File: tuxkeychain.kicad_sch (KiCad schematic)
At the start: 45 parts, among them J1 Amphenol_10104111, Q2 2N7002, SW1 B3U-1000P, U1 JW5211, U2 JW5211, U3 JW5211, U4 F1C100s, U6 W25Q128JVS, Y1 24MHz

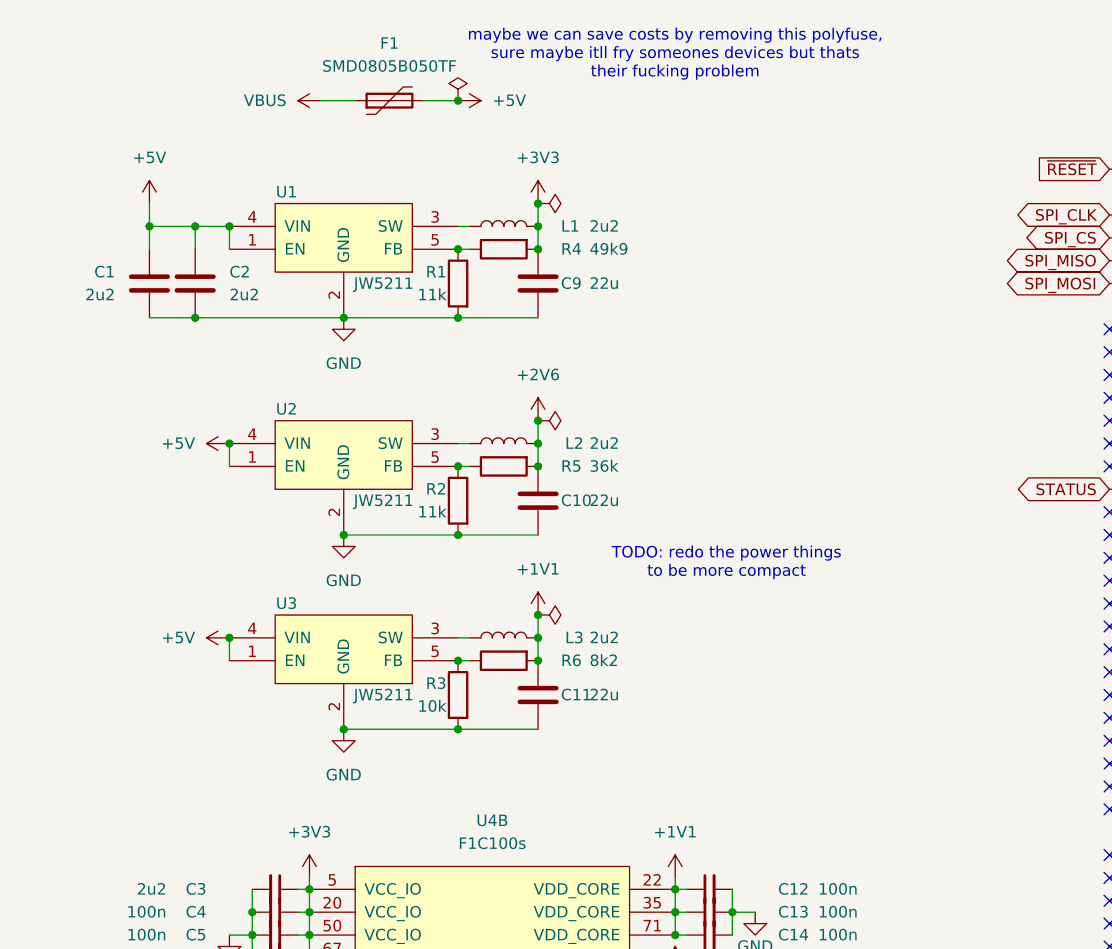
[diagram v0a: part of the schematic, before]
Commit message: Change regulators to the TLV76701DRVx due to supply chain issues
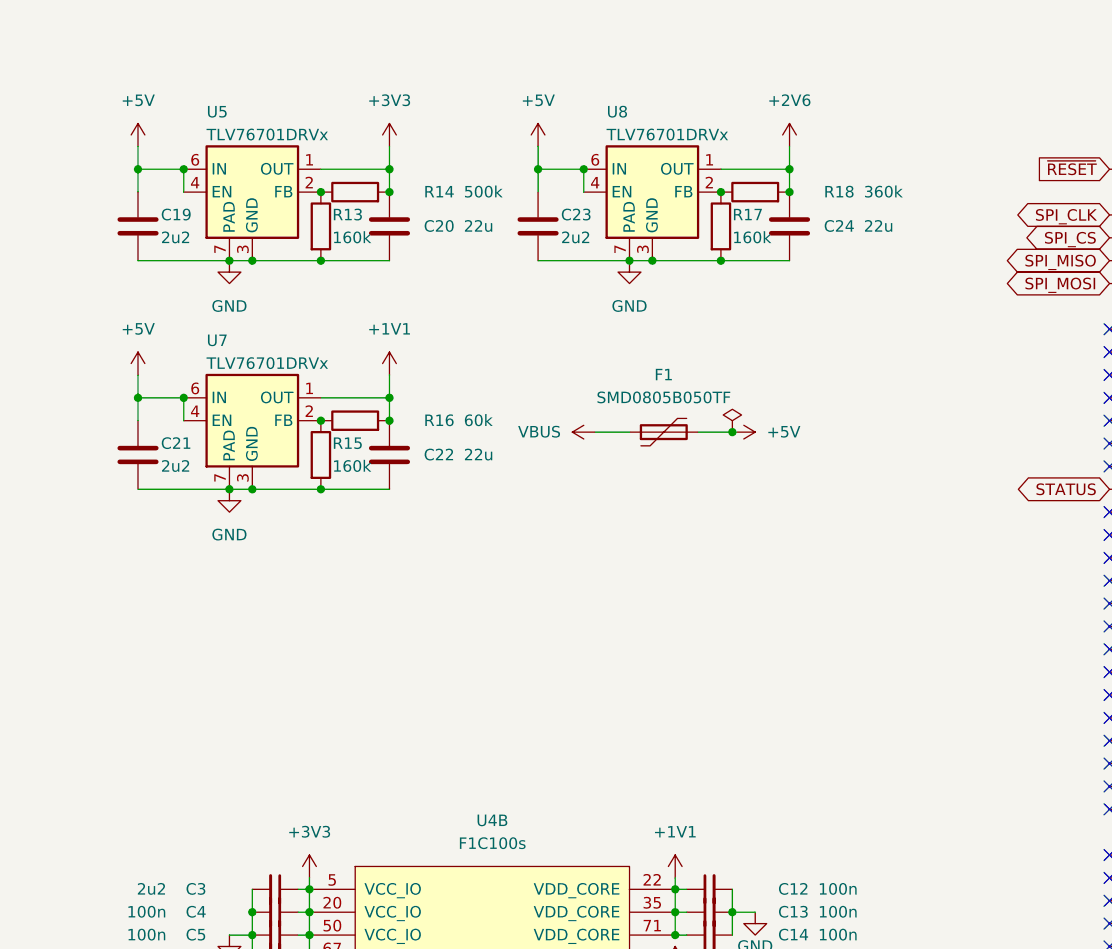
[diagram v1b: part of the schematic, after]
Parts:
- removed C1, C2: 2u2, Capacitor_SMD:C_0603_1608Metric, symbol Device:C
- removed C10, C11, C9: 22u, Capacitor_SMD:C_0603_1608Metric, symbol Device:C
- removed L1, L2, L3: 2u2, Inductor_SMD:L_0805_2012Metric, symbol Device:L
- removed R1, R2: 11k, Resistor_SMD:R_0603_1608Metric, symbol Device:R
- removed R3: 10k, Resistor_SMD:R_0603_1608Metric, symbol Device:R
- removed R4: 49k9, Resistor_SMD:R_0603_1608Metric, symbol Device:R
- removed R5: 36k, Resistor_SMD:R_0603_1608Metric, symbol Device:R
- removed R6: 8k2, Resistor_SMD:R_0603_1608Metric, symbol Device:R
- removed U1, U2, U3: JW5211, Package_TO_SOT_SMD:SOT-23-5, symbol tuxkeychain:JW5211
- added C19, C21, C23: 2u2, Capacitor_SMD:C_0603_1608Metric, symbol Device:C
- added C20, C22, C24: 22u, symbol Device:C
- added R13, R15, R17: 160k, symbol Device:R
- added R14: 500k, symbol Device:R
- added R16: 60k, symbol Device:R
- added R18: 360k, symbol Device:R
- added U5, U7, U8: TLV76701DRVx, Package_SON:WSON-6-1EP_2x2mm_P0.65mm_EP1x1.6mm, symbol Regulator_Linear:TLV76701DRVx
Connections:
- net +1V1: now also C22.1, R16.2, U7.1 (OUT)
- net +2V6: now also C24.1, R18.2, U8.1 (OUT)
- net +3V3: now also C20.1, R14.2, U5.1 (OUT)
- net +5V: now also C19.1, C21.1, C23.1, U5.4 (EN), U5.6 (IN), U7.4 (EN), U7.6 (IN), U8.4 (EN), U8.6 (IN)
- net GND: now also C19.2, C20.2, C21.2, C22.2, C23.2, C24.2, R13.2, R15.2, R17.2, U5.3 (GND), U5.5 (GND), U5.7 (PAD), U7.3 (GND), U7.5 (GND), U7.7 (PAD), U8.3 (GND), U8.5 (GND), U8.7 (PAD)
- new net: R13.1, R14.1, U5.2 (FB)
- new net: R17.1, R18.1, U8.2 (FB)
- new net: R15.1, R16.1, U7.2 (FB)
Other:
- note removed: "TODO: redo the power things to be more compact"
- note removed: "maybe we can save costs by removing this polyfuse, sure maybe itll fry someones devices but thats their fucking problem"
- moved on the sheet: F1

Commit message: bump rev
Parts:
- removed C19, C21, C23: 2u2, Capacitor_SMD:C_0603_1608Metric, symbol Device:C
- removed C20, C22, C24: 22u, symbol Device:C
- removed R13, R15, R17: 160k, symbol Device:R
- removed R14: 500k, symbol Device:R
- removed R16: 60k, symbol Device:R
- removed R18: 360k, symbol Device:R
- removed U5, U7, U8: TLV76701DRVx, Package_SON:WSON-6-1EP_2x2mm_P0.65mm_EP1x1.6mm, symbol Regulator_Linear:TLV76701DRVx
- added C1, C2: 2u2, Capacitor_SMD:C_0603_1608Metric, symbol Device:C
- added C10, C11, C9: 22u, Capacitor_SMD:C_0603_1608Metric, symbol Device:C
- added L1, L2, L3: 2u2, Inductor_SMD:L_0805_2012Metric, symbol Device:L
- added R1, R2: 11k, Resistor_SMD:R_0603_1608Metric, symbol Device:R
- added R3: 10k, Resistor_SMD:R_0603_1608Metric, symbol Device:R
- added R4: 49k9, Resistor_SMD:R_0603_1608Metric, symbol Device:R
- added R5: 36k, Resistor_SMD:R_0603_1608Metric, symbol Device:R
- added R6: 8k2, Resistor_SMD:R_0603_1608Metric, symbol Device:R
- added U1, U2, U3: JW5211, Package_TO_SOT_SMD:SOT-23-5, symbol tuxkeychain:JW5211
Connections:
- net +1V1: now also C11.1, L3.2, R6.2
- net +2V6: now also C10.1, L2.2, R5.2
- net +3V3: now also C9.1, L1.2, R4.2
- net +5V: now also C1.1, C2.1, U1.1 (EN), U1.4 (VIN), U2.1 (EN), U2.4 (VIN), U3.1 (EN), U3.4 (VIN)
- net GND: now also C1.2, C10.2, C11.2, C2.2, C9.2, R1.2, R2.2, R3.2, U1.2 (GND), U2.2 (GND), U3.2 (GND)
- new net: L2.1, U2.3 (SW)
- new net: R1.1, R4.1, U1.5 (FB)
- new net: R3.1, R6.1, U3.5 (FB)
- new net: L1.1, U1.3 (SW)
- new net: L3.1, U3.3 (SW)
- new net: R2.1, R5.1, U2.5 (FB)
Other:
- note added: "TODO: redo the power things to be more compact"
- note added: "maybe we can save costs by removing this polyfuse, sure maybe itll fry someones devices but thats their fucking problem"
- moved on the sheet: F1

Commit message: Revert "bump rev"
This reverts commit ef9e417096638242890c258b05ee16d024b64b77.
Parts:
- removed C1, C2: 2u2, Capacitor_SMD:C_0603_1608Metric, symbol Device:C
- removed C10, C11, C9: 22u, Capacitor_SMD:C_0603_1608Metric, symbol Device:C
- removed L1, L2, L3: 2u2, Inductor_SMD:L_0805_2012Metric, symbol Device:L
- removed R1, R2: 11k, Resistor_SMD:R_0603_1608Metric, symbol Device:R
- removed R3: 10k, Resistor_SMD:R_0603_1608Metric, symbol Device:R
- removed R4: 49k9, Resistor_SMD:R_0603_1608Metric, symbol Device:R
- removed R5: 36k, Resistor_SMD:R_0603_1608Metric, symbol Device:R
- removed R6: 8k2, Resistor_SMD:R_0603_1608Metric, symbol Device:R
- removed U1, U2, U3: JW5211, Package_TO_SOT_SMD:SOT-23-5, symbol tuxkeychain:JW5211
- added C19, C21, C23: 2u2, Capacitor_SMD:C_0603_1608Metric, symbol Device:C
- added C20, C22, C24: 22u, symbol Device:C
- added R13, R15, R17: 160k, symbol Device:R
- added R14: 500k, symbol Device:R
- added R16: 60k, symbol Device:R
- added R18: 360k, symbol Device:R
- added U5, U7, U8: TLV76701DRVx, Package_SON:WSON-6-1EP_2x2mm_P0.65mm_EP1x1.6mm, symbol Regulator_Linear:TLV76701DRVx
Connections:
- net +1V1: now also C22.1, R16.2, U7.1 (OUT)
- net +2V6: now also C24.1, R18.2, U8.1 (OUT)
- net +3V3: now also C20.1, R14.2, U5.1 (OUT)
- net +5V: now also C19.1, C21.1, C23.1, U5.4 (EN), U5.6 (IN), U7.4 (EN), U7.6 (IN), U8.4 (EN), U8.6 (IN)
- net GND: now also C19.2, C20.2, C21.2, C22.2, C23.2, C24.2, R13.2, R15.2, R17.2, U5.3 (GND), U5.5 (GND), U5.7 (PAD), U7.3 (GND), U7.5 (GND), U7.7 (PAD), U8.3 (GND), U8.5 (GND), U8.7 (PAD)
- new net: R13.1, R14.1, U5.2 (FB)
- new net: R17.1, R18.1, U8.2 (FB)
- new net: R15.1, R16.1, U7.2 (FB)
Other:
- note removed: "TODO: redo the power things to be more compact"
- note removed: "maybe we can save costs by removing this polyfuse, sure maybe itll fry someones devices but thats their fucking problem"
- moved on the sheet: F1
